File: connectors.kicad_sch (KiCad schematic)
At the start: 42 parts, among them CN102 Expansion, CN901 HuCARD, CN902 JOY1

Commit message: First draft complete.
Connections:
- net DIN_L: now also L601.1; no longer L602.1
- net DIN_R: now also L602.1; no longer L601.1
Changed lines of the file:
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@@
     )
   )
-  (global_label "DIN_R" (shape input) (at 243.205 222.25 0) (fields_autoplaced)
-    (effects (font (size 1.27 1.27)) (justify left))
-    (property "Intersheetrefs" "${INTERSHEET_REFS}" (at 251.6331 222.25 0)
-      (effects (font (size 1.27 1.27)) (justify left) hide)
+  (global_label "DIN_R" (shape input) (at 184.15 224.79 180) (fields_autoplaced)
+    (effects (font (size 1.27 1.27)) (justify right))
+    (property "Intersheetrefs" "${INTERSHEET_REFS}" (at 175.7219 224.79 0)
+      (effects (font (size 1.27 1.27)) (justify right) hide)
     )
   )
@@
     )
   )
-  (global_label "DIN_L" (shape input) (at 184.15 224.79 180) (fields_autoplaced)
-    (effects (font (size 1.27 1.27)) (justify right))
-    (property "Intersheetrefs" "${INTERSHEET_REFS}" (at 175.9638 224.79 0)
-      (effects (font (size 1.27 1.27)) (justify right) hide)
+  (global_label "DIN_L" (shape input) (at 243.205 222.25 0) (fields_autoplaced)
+    (effects (font (size 1.27 1.27)) (justify left))
+    (property "Intersheetrefs" "${INTERSHEET_REFS}" (at 251.3912 222.25 0)
+      (effects (font (size 1.27 1.27)) (justify left) hide)
     )
   )

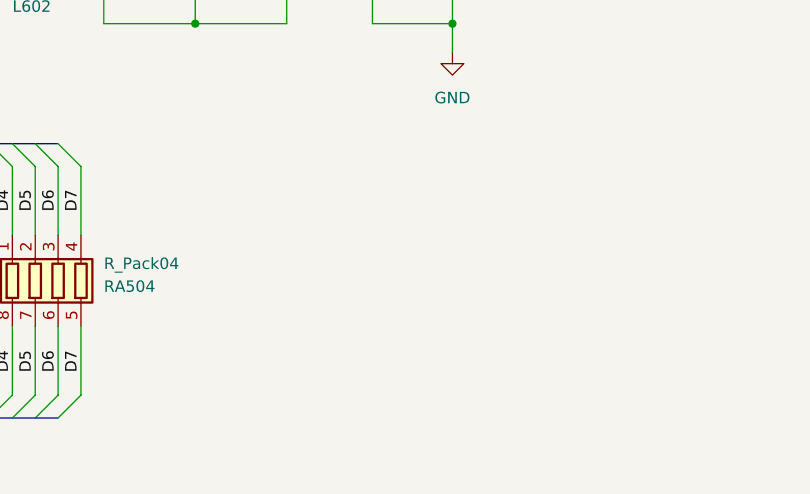
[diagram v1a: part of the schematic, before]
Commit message: Fix DRC errors.
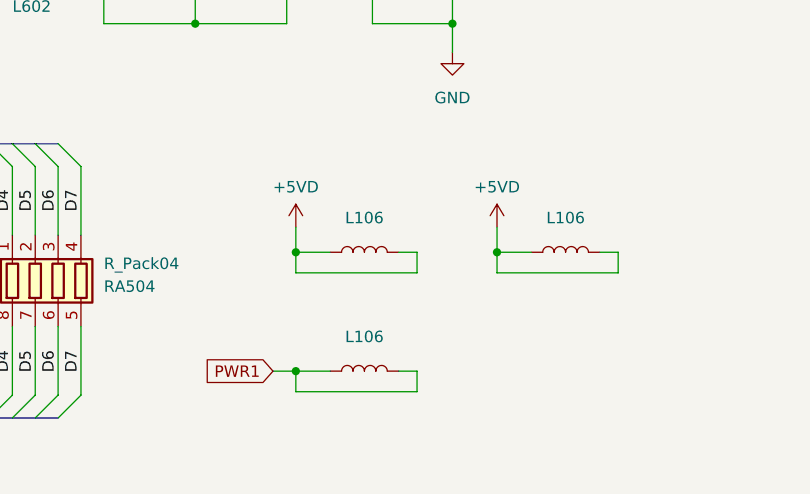
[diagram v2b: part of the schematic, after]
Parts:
- added L106 (x3): ~, A-PCENGINE:SMD_0805_Narrow_Long, symbol Device:L
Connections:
- net +5VD: now also L106.1, L106.1, L106.2, L106.2
- new net PWR1: L106.1, L106.2

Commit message: General clean-up.
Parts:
- removed CN102: Expansion, A-PCENGINE:CN102-2.54mm, symbol PC-Engine:Conn_03x23
- added L106: ~, A-PCENGINE:SMD_0805_Narrow_Long, symbol Device:L
- added L106 (x2): ~, A-PCENGINE:SMD_1806, symbol Device:L
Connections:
- net +5V: now also L106.1, L106.1, L106.2, L106.2
- net +5VD: now also L106.1, L106.2
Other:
- note added: "Extra unused/non-functional footprints"
- note removed: "Shield on underside connects these pins to ground"
- moved on the sheet: C944, CN901, CN902, FL107, JK601, JP1, JP10, JP11, JP12, JP13, JP14, JP15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

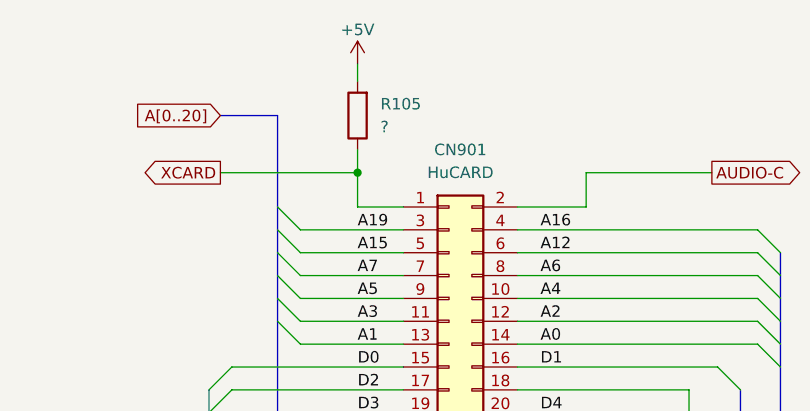
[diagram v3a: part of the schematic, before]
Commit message: Add resistor values to schematics.
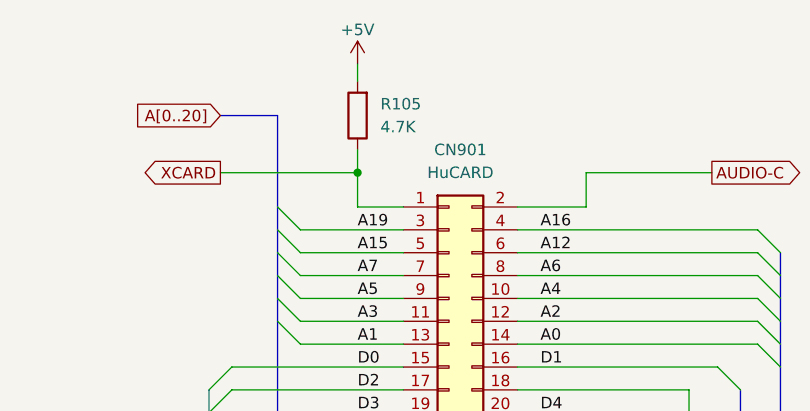
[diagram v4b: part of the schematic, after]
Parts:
- R105: value ? -> 4.7K
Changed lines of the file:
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@@
       (effects (font (size 1.27 1.27)) (justify right))
     )
-    (property "Value" "?" (at 116.078 40.894 0)
+    (property "Value" "4.7K" (at 116.078 40.894 0)
       (effects (font (size 1.27 1.27)) (justify right))
     )

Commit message: Intermediate commit after renaming some nets.
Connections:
- net CFX3: now also JP10.1 (A), JP10.2 (B), JP9.1 (A), JP9.2 (B); no longer JP1.1 (A), JP1.2 (B), JP2.1 (A), JP2.2 (B)
- net CFX4: now also JP7.1 (A), JP7.2 (B), JP8.1 (A), JP8.2 (B); no longer JP3.1 (A), JP3.2 (B), JP4.1 (A), JP4.2 (B)
- net CFX6: now also JP3.1 (A), JP3.2 (B), JP4.1 (A), JP4.2 (B); no longer JP7.1 (A), JP7.2 (B), JP8.1 (A), JP8.2 (B)
- net CFX7: now also JP1.1 (A), JP1.2 (B), JP2.1 (A), JP2.2 (B); no longer JP10.1 (A), JP10.2 (B), JP9.1 (A), JP9.2 (B)
- net CFX10 renamed CFX0
- net CFX8 renamed CFX2
- net CFX9 renamed CFX1

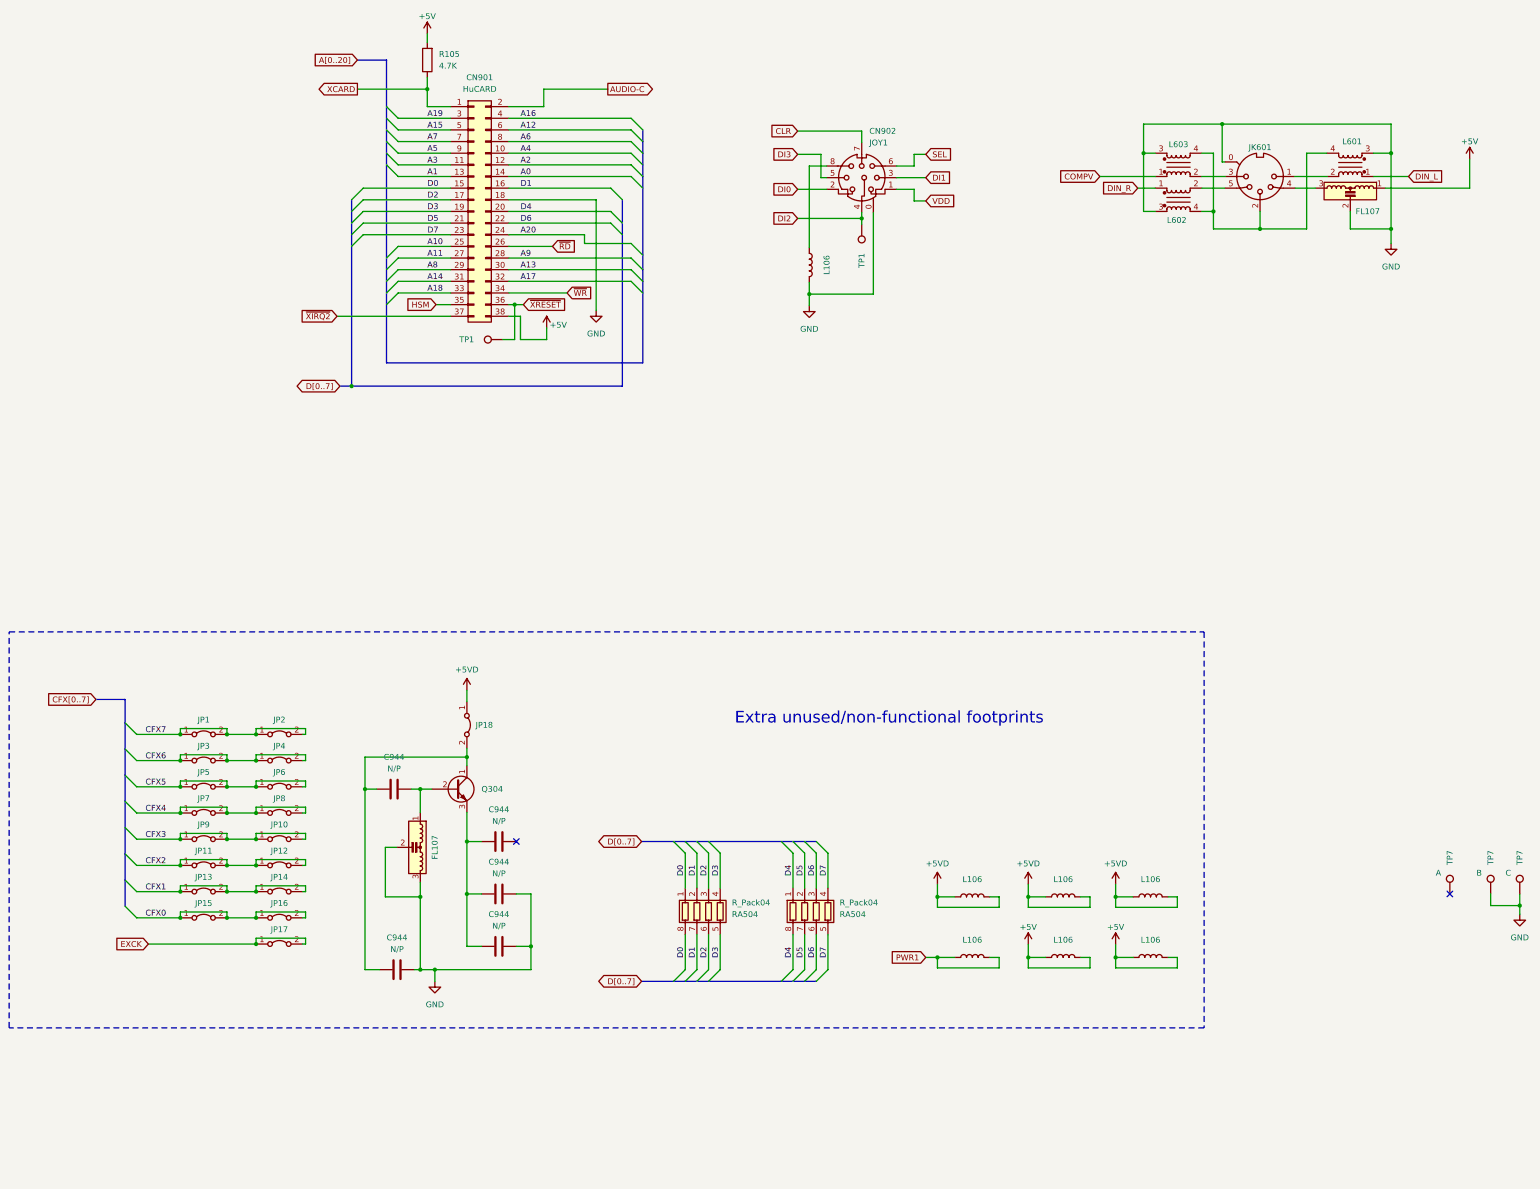
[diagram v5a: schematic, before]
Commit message: Schematic clean-up (IFU ASIC and other stuff).
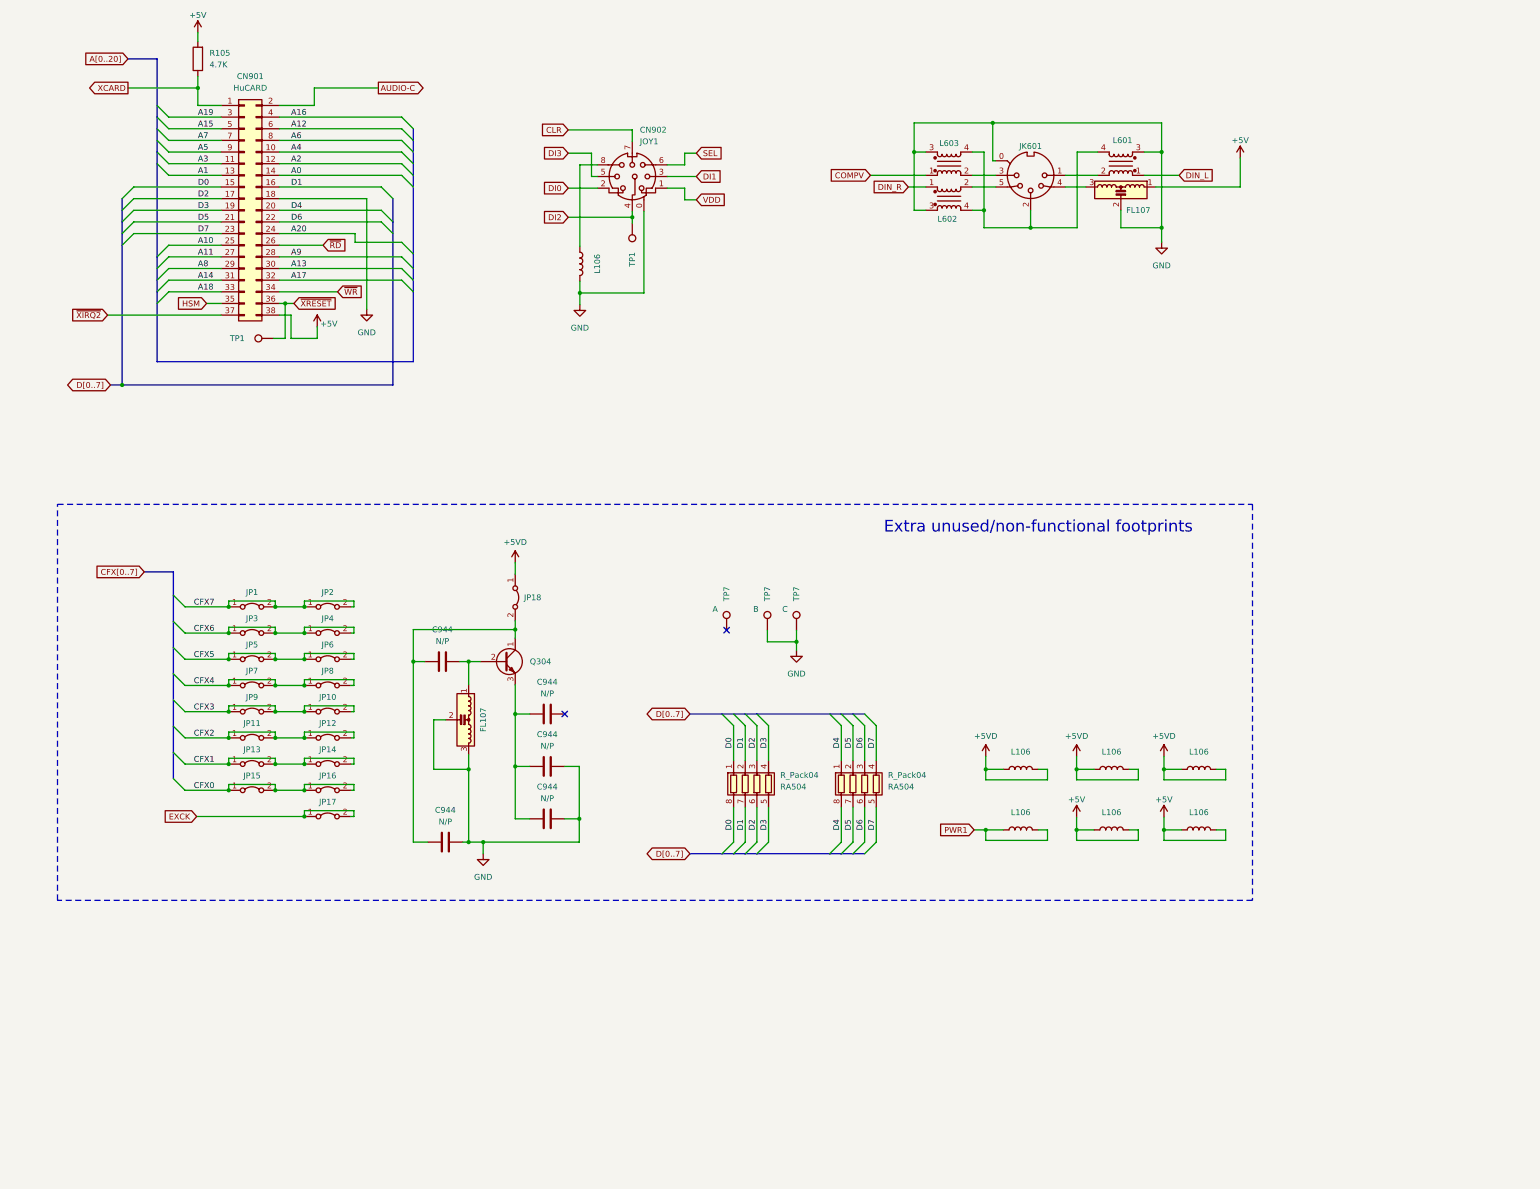
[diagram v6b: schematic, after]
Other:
- moved on the sheet: C944, CN901, CN902, FL107, JK601, JP1, JP10, JP11, JP12, JP13, JP14, JP15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
